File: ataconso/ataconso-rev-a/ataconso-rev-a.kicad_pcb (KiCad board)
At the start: 2 copper layers, 89 x 51 mm, 17 parts, among them J1 Screw_Terminal_01x02, J2 Barrel_Jack_Switch, SW1 SW_SPDT, U1 NE555D, U2 NE555D

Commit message: corregir nombre
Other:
- board text added: "ataconso"
- board text removed: "atariconso"

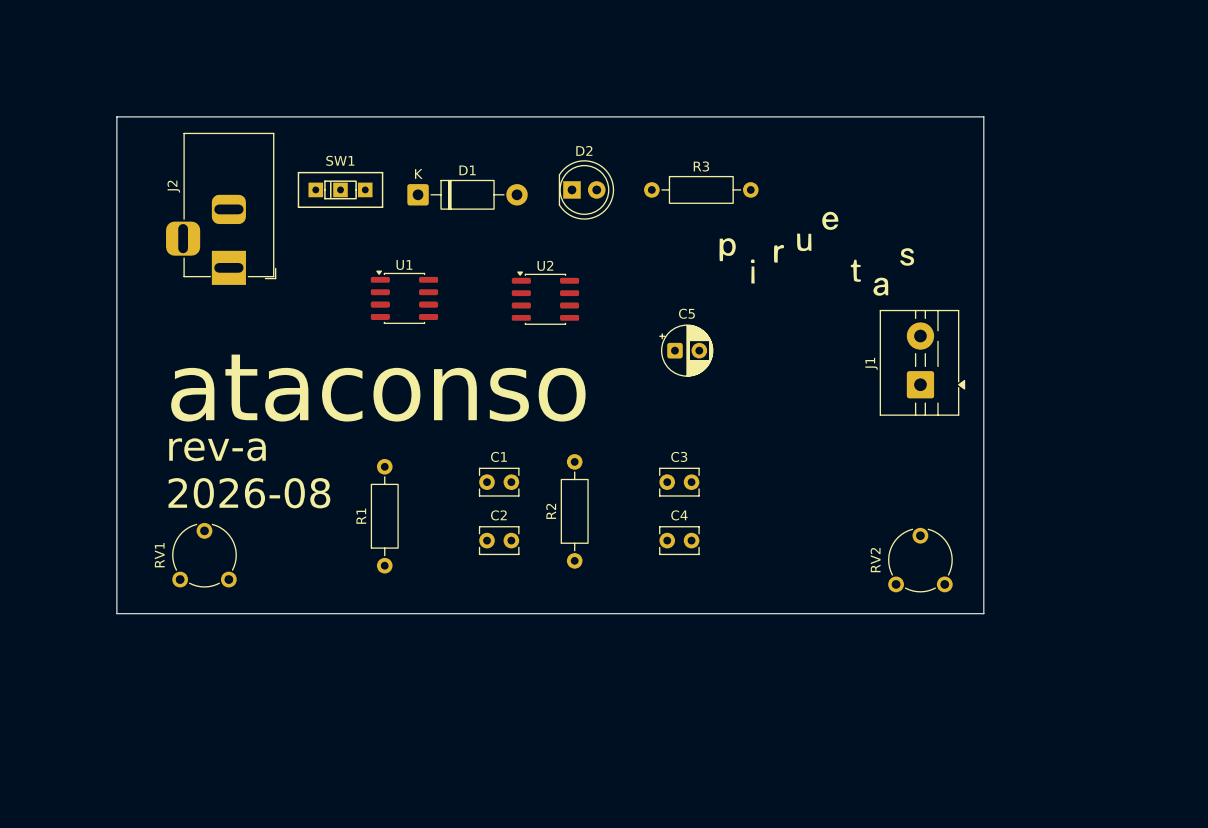
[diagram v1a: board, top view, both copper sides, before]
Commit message: agregar vias de 0.8mm
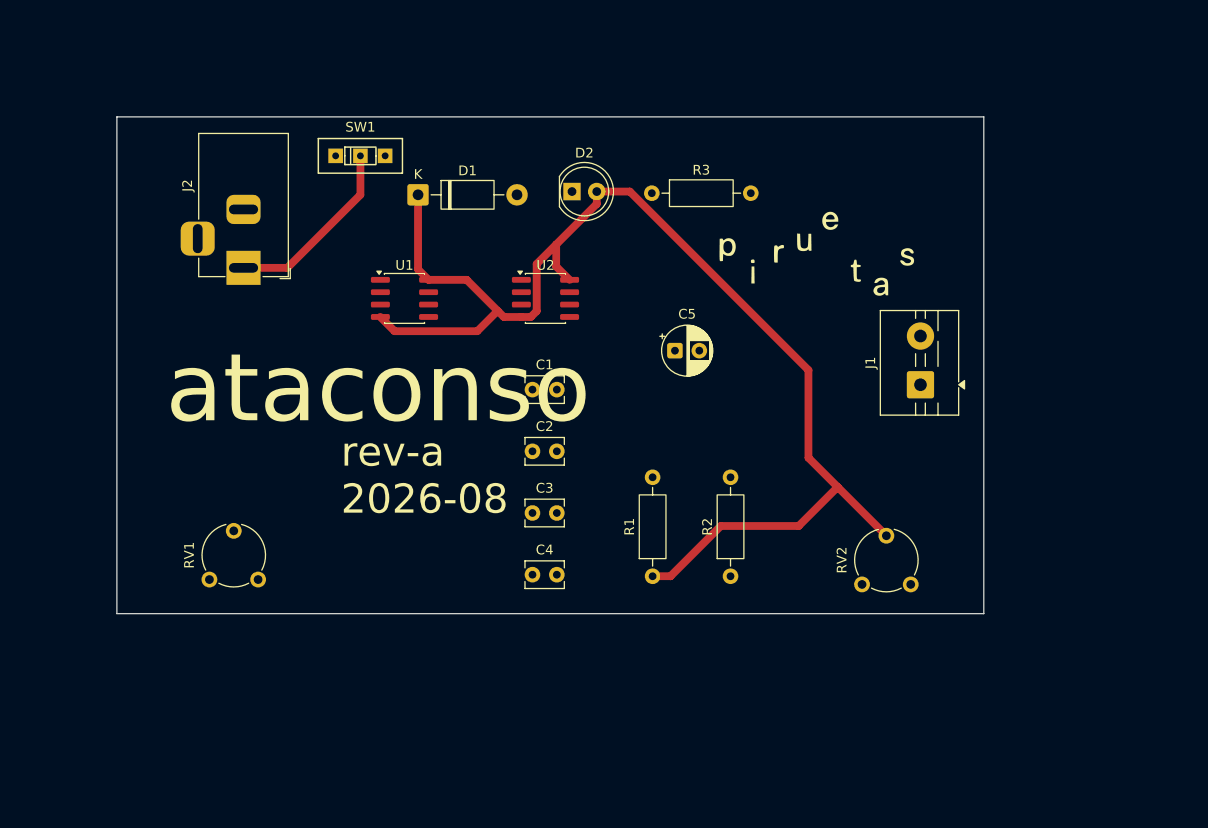
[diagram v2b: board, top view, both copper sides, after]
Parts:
- moved R1 27.5 mm to (105.0, 97.2)
- moved R2 16.1 mm to (113.0, 97.2)
- moved C4 14.3 mm to (92.7, 97.0)
- moved C3 14.2 mm to (92.7, 90.7)
- moved C1 10.6 mm to (92.7, 78.0)
- moved C2 10.3 mm to (92.7, 84.3)
- moved SW1 4.05 mm to (75.0, 54.0)
- moved RV2 3.50 mm to (131.5, 98.0)
- moved RV1 3.01 mm to (64.5, 97.5)
- moved J2 1.50 mm to (63.0, 65.5)
- moved R3 0.33 mm to (104.9, 57.8)
- moved D2 0.17 mm to (96.7, 57.7)
- moved U2 0.09 mm to (94.0, 68.6)
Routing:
- net VCC: track 0.00 -> 127.1 mm
- net Net-(SW1-B): track 0.00 -> 19.1 mm

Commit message: agregar primera version
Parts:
- added H1: MountingHole, MountingHole:MountingHole_3.2mm_M3, F.Cu at (54.0, 95.0)
- added H2: MountingHole, MountingHole:MountingHole_3.2mm_M3, F.Cu at (134.0, 55.0)
- moved R1 25.0 mm to (80.1, 95.0), turned to 180 degrees
- moved C3 12.7 mm to (94.0, 78.0)
- moved C4 12.7 mm to (94.0, 84.3)
- moved C2 6.18 mm to (86.5, 84.0)
- moved C1 6.17 mm to (86.5, 78.0)
- moved R2 4.16 mm to (113.1, 93.0), turned to 180 degrees
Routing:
- net Net-(U1-THRES): track 0.00 -> 60.1 mm
- net Net-(U1-OUT): track 0.00 -> 46.8 mm
- net Net-(U1-DISCH): track 0.00 -> 44.9 mm, vias 0 -> 1
- net Net-(U2-DISCH): track 0.00 -> 30.3 mm
- net VCC: track 127.1 -> 153.1 mm
- net Net-(J1-Pin_1): track 0.00 -> 24.2 mm
- net Net-(U2-OUT): track 0.00 -> 24.1 mm
- net Net-(U2-CONT): track 0.00 -> 16.9 mm
- net Net-(R2-Pad1): track 0.00 -> 15.5 mm
- net Net-(U1-CONT): track 0.00 -> 15.3 mm
- net Net-(D1-A): track 0.00 -> 15.2 mm
- net Net-(D2-K): track 0.00 -> 12.1 mm
- net Net-(SW1-B): track 19.1 -> 18.5 mm
- added copper zone on B.Cu, net GND
- added copper zone on F.Cu, net GND
